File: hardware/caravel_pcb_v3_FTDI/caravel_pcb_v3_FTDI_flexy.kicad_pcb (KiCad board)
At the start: 2 copper layers, 76.2 x 70.2 mm, 60 parts, among them J1 USB_B_Micro - 10118193-0001LF, J10 Conn_01x27_Female, J11 Conn_01x20_Female, J2 Conn_01x02_Female, J3 Conn_01x02_Female, J5 Conn_01x02_Male, J6 Conn_01x02_Male, J7 Conn_01x06_Female, J8 Conn_01x02_Male, J9 Conn_01x02_Male, SW1 SW_Push - SKQGADE010, T1 Logo, T2 Logo, U1 FT232H, U2 SN74LVC1G125DCKR, U3 SN74LVC1G125DCKR, U4 AZ1117CH-1.8TRG1, U5 AZ1117-3.3, U6 caravel_breakout, U7 W25Q32FVSS, X1 DSC6001_10MHZ, Y1 CSTNE12M0GH5L000R0

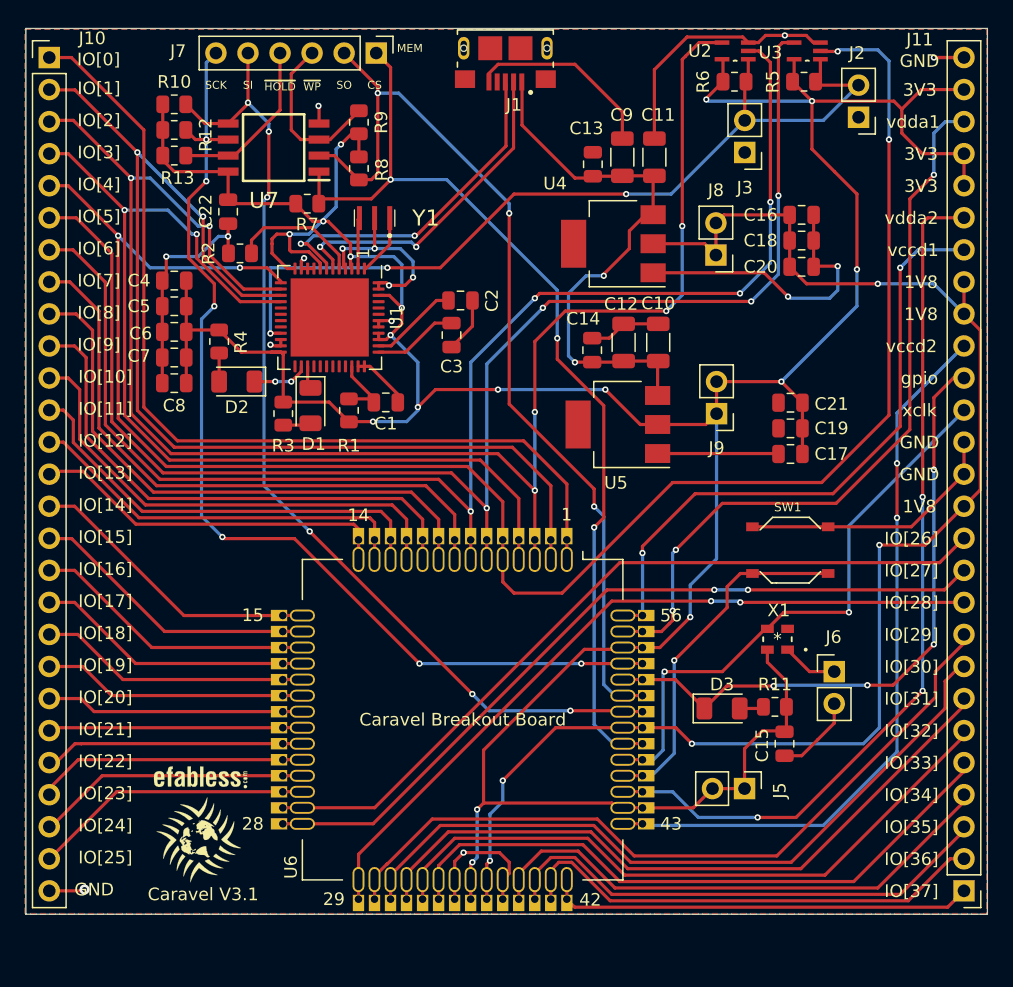
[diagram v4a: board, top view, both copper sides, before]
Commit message: update FTDI caravel board PCB and BOM (Rev 3C)
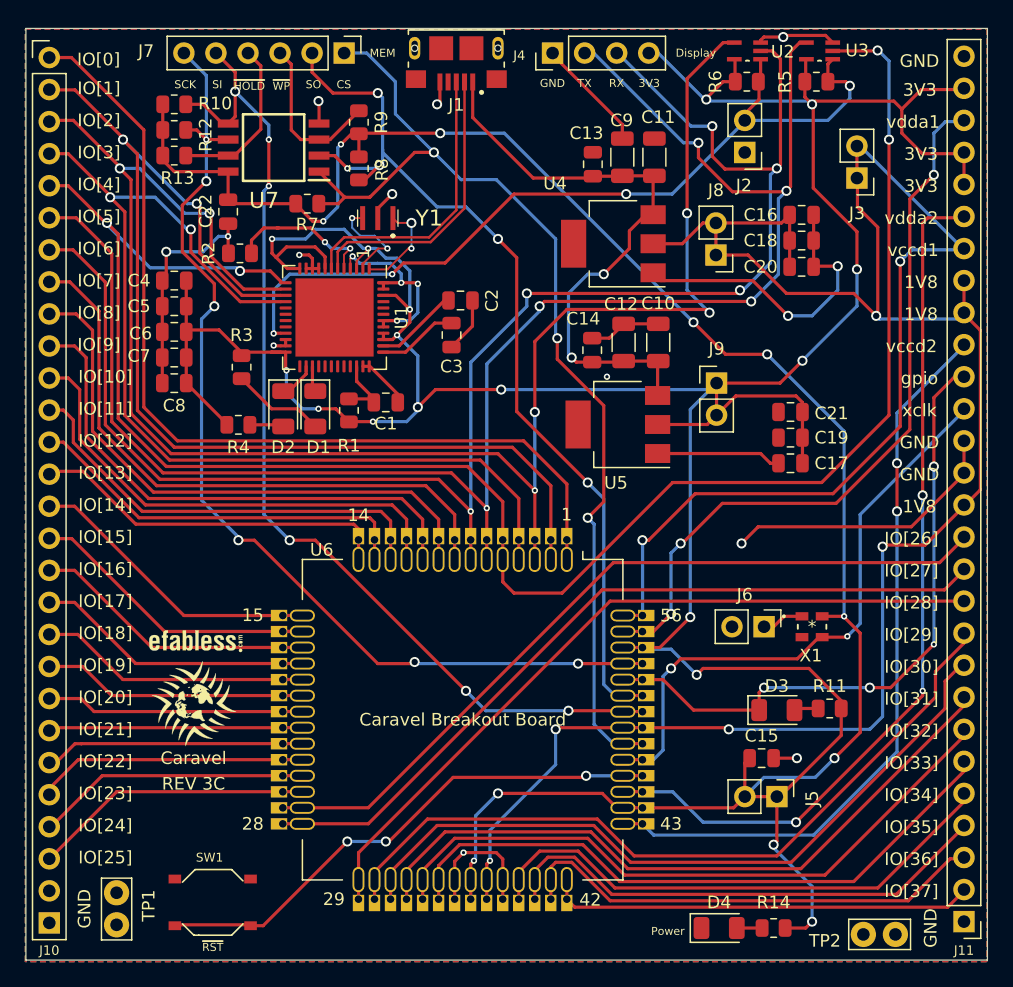
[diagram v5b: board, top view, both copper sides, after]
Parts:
- added D4: LED - 17-215SURC/S530-A2/TR8, LED_SMD:LED_1206_3216Metric, F.Cu at (154.9, 130.0)
- added J4: Conn_01x04_Female, Connector_PinHeader_2.54mm:PinHeader_1x04_P2.54mm_Vertical, F.Cu at (141.7, 60.7)
- added R14: 82 - 0805W8F820JT5E, Resistor_SMD:R_0805_2012Metric, F.Cu at (159.3, 130.0)
- added TP1: TestPoint, TestPoint:TestPoint_Bridge_Pitch2.54mm_Drill1.0mm, F.Cu at (107.2, 129.8)
- added TP2: TestPoint, TestPoint:TestPoint_Bridge_Pitch2.54mm_Drill1.0mm, F.Cu at (168.9, 130.6)
- J10, J11: footprint Connector_PinHeader_2.54mm:PinHeader_1x27_P2.54mm_Vertical -> Connector_PinHeader_2.54mm:PinHeader_1x28_P2.54mm_Vertical
- J3: value Conn_01x02_Female -> Conn_01x02_Male
- moved SW1 53.6 mm to (114.8, 128.0)
- moved T1 10.8 mm to (113.3, 112.3)
- moved T2 10.8 mm to (113.4, 107.3)
- moved J2 9.44 mm to (157.0, 68.6)
- moved J3 9.12 mm to (165.9, 70.6)
- moved R4 6.78 mm to (116.8, 90.2), turned to 180 degrees
- moved J6 6.60 mm to (158.5, 106.2), turned to -90 degrees
- moved R3 4.95 mm to (117.1, 85.6)
- moved D3 4.34 mm to (159.5, 112.8)
- moved R11 4.34 mm to (163.7, 112.6)
- moved D2 4.27 mm to (120.4, 88.9), turned to -90 degrees
- moved J1 3.89 mm to (134.1, 60.3)
- moved X1 2.91 mm to (162.3, 106.2), turned to 0 degrees
- moved J5 2.64 mm to (159.5, 119.6)
- moved J7 2.54 mm to (125.2, 60.7)
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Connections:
- C16 pad 2: vccd -> vccd1
- C18 pad 2: vccd -> vccd1
- C20 pad 2: vccd -> vccd1
- J11 pad 1: mprj_io[37] -> GND
- J11 pad 10: mprj_io[28] -> mprj_io[29]
- J11 pad 11: mprj_io[27] -> mprj_io[28]
- J11 pad 12: mprj_io[26] -> mprj_io[27]
- J11 pad 13: vccd -> mprj_io[26]
- J11 pad 14: GND -> vccd1
- J11 pad 16: xclk -> GND
- J11 pad 17: gpio -> xclk
- J11 pad 18: vccd2 -> gpio
- J11 pad 19: vccd -> vccd2
- J11 pad 2: mprj_io[36] -> mprj_io[37]
- J11 pad 20: vccd -> vccd1
- J11 pad 22: vdda2 -> vccd1
- J11 pad 23: vdda -> vdda2
- J11 pad 25: vdda1 -> vdda
- J11 pad 26: vdda -> vdda1
- J11 pad 27: GND -> vdda
- J11 pad 3: mprj_io[35] -> mprj_io[36]
- J11 pad 4: mprj_io[34] -> mprj_io[35]
- J11 pad 5: mprj_io[33] -> mprj_io[34]
- J11 pad 6: mprj_io[32] -> mprj_io[33]
- J11 pad 7: mprj_io[31] -> mprj_io[32]
- J11 pad 8: mprj_io[30] -> mprj_io[31]
- J11 pad 9: mprj_io[29] -> mprj_io[30]
- J3 pad 1: GND -> vccd1
- J3 pad 2: UART_EN -> vccd1
- J8 pad 1: vccd -> vccd1
- J8 pad 2: vccd -> vccd1
- U4 pad 2: vccd -> vccd1
- U6 pad 37: vccd -> vccd1
- U6 pad 49: vccd -> vccd1
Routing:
- net vccd1: track 49.9 -> 198.6 mm, vias 2 -> 7
- net vdda: track 292.6 -> 417.5 mm, vias 17 -> 26
- net vccd: track 117.4 -> 0.00 mm, vias 5 -> 0
- net GND: track 168.9 -> 143.2 mm, vias 16 -> 18
- net mprj_io[5]_ser_rx: track 113.0 -> 134.6 mm, vias 4 -> 5
- net mprj_io[6]_ser_tx: track 109.3 -> 128.1 mm, vias 4 -> 5
- net ~{RST}: track 28.3 -> 42.0 mm, vias 1 -> 3
- net Caravel_CSB: track 77.1 -> 82.5 mm
- net USB_SO_RXD: track 131.3 -> 136.7 mm
- net Net-(D1-Pad2): track 2.22 -> 7.41 mm
- net FTDI_D+: track 27.4 -> 22.8 mm, vias 2 -> 0
- net Net-(U1-Pad2): track 4.02 -> 7.90 mm, vias 0 -> 2
- net FTDI_D-: track 26.3 -> 22.8 mm, vias 2 -> 0
- net +5V: track 44.1 -> 47.5 mm
- net Net-(U1-Pad1): track 4.64 -> 7.71 mm, vias 0 -> 2
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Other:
- board size 76.2 x 70.2 mm -> 76.2 x 73.8 mm
- board text added: "Caravel"
- board text added: "Display"
- board text added: "Power"
- board text added: "REV 3C"
- board text added: "RX"
- board text added: "TX"
- board text added: "~{RST}"
- board text removed: "Caravel V3.1"

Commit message: update FTDI caravel board PCB (Rev 3D)
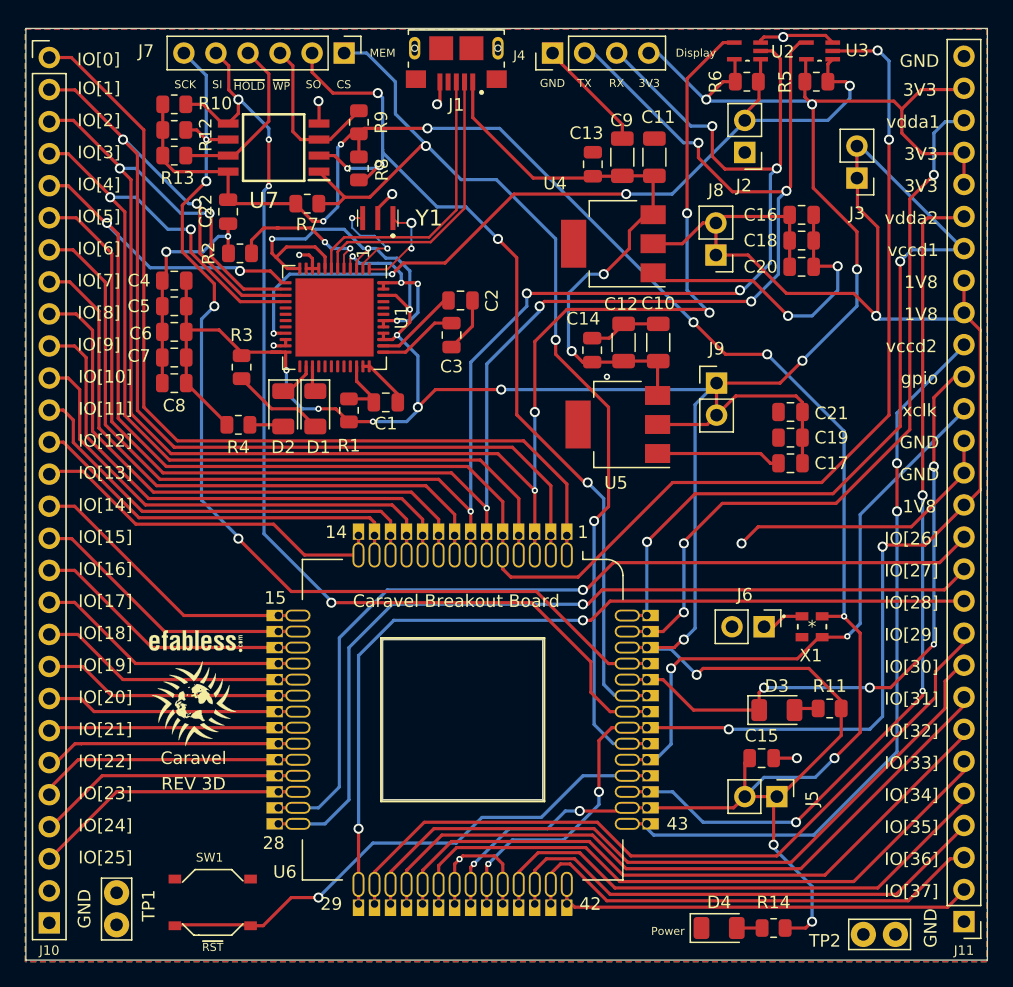
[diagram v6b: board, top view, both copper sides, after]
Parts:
- U6: footprint Caravel_Board:caravel_breakout_flexy -> Caravel_Board:caravel_breakout_flexy_rev3D
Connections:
- net vccd1 renamed vccd
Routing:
- net mprj_io[28]: track 59.9 -> 69.1 mm, vias 0 -> 2
- net mprj_io[27]: track 62.3 -> 69.7 mm, vias 0 -> 1
- net mprj_io[26]: track 62.8 -> 70.1 mm, vias 0 -> 1
- net vdda: track 417.5 -> 415.1 mm
- net Caravel_D0: track 81.5 -> 84.0 mm, vias 6 -> 4
- net USB_SCK_TXD: track 146.8 -> 145.2 mm
- net vccd: track 198.6 -> 198.1 mm
- net GND: track 143.2 -> 142.6 mm
- net ~{MEM_HOLD}: track 13.3 -> 13.8 mm
- net Caravel_SCK: track 82.7 -> 82.5 mm, vias 6 -> 4
- net ~{RST}: vias 3 -> 1
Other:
- board text added: "REV 3D"
- board text removed: "56"
- board text removed: "REV 3C"
